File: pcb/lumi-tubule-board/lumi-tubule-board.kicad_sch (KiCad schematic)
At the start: 44 parts, among them SW1 SWITCH_TACT_SMT4.6X2.8, SW2 SWITCH_TACT_SMT4.6X2.8, U1 SHTC3, U2 VREG_SOT23-5, U3 ESP32-S3-MINI-1, U4 LIS2Dx12, U5 TLC59108xPW, U6 TLC59108xPW, X1 USB_C

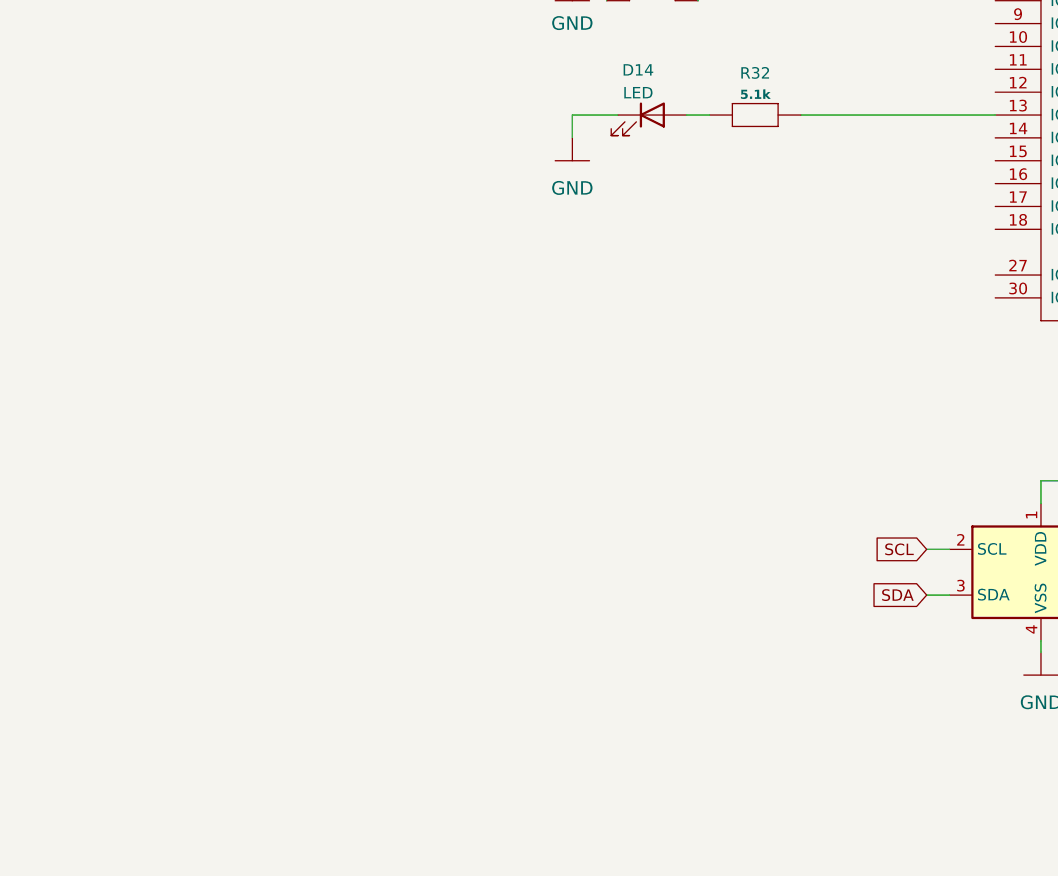
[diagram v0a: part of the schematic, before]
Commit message: Add USB data/power splitter board
Add a small separate (mousebites) USB power/data splitter board. Fits neatly within the central cutout of the main board.
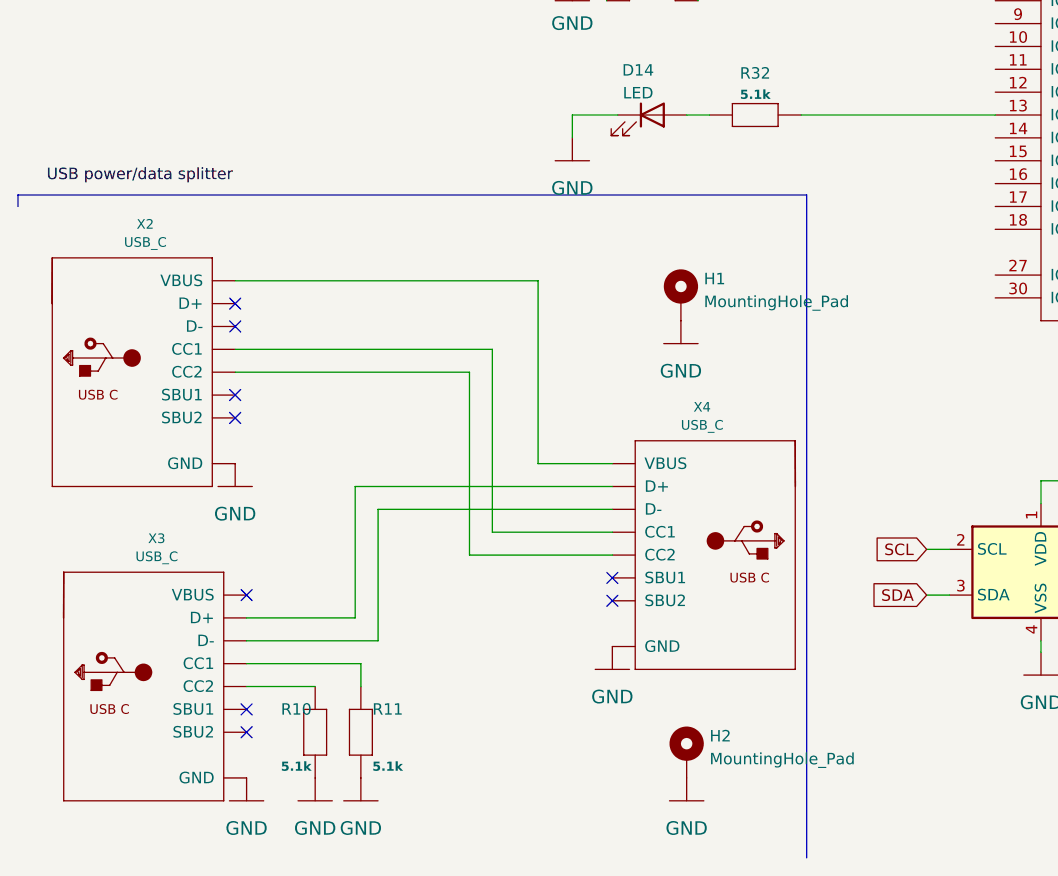
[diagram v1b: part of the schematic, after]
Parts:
- added H1, H2: MountingHole_Pad, symbol Mechanical:MountingHole_Pad
- added R10, R11: 5.1k, Resistor_SMD:R_0603_1608Metric, symbol Adafruit_ESP32-S3_8MB_No_PSRAM-eagle-import:RESISTOR_0603
- added X2, X3, X4: USB_C, Connector_USB:USB_C_Receptacle_HRO_TYPE-C-31-M-12, symbol Adafruit_ESP32-S3_8MB_No_PSRAM-eagle-import:USB_C
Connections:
- net GND: now also H1.1, H2.1, R10.2, R11.2, X2.A1 (GND), X2.A12 (GND), X2.B1 (GND), X2.B12 (GND), X3.A1 (GND), X3.A12 (GND), X3.B1 (GND), X3.B12 (GND), X4.A1 (GND), X4.A12 (GND), X4.B1 (GND), X4.B12 (GND)
- new net: X2.A4 (VBUS), X2.A9 (VBUS), X2.B4 (VBUS), X2.B9 (VBUS), X4.A4 (VBUS), X4.A9 (VBUS), X4.B4 (VBUS), X4.B9 (VBUS)
- new net: X2.A5 (CC1), X4.A5 (CC1)
- new net: X3.A6 (D+), X3.B6 (D+), X4.A6 (D+), X4.B6 (D+)
- new net: X3.A7 (D-), X3.B7 (D-), X4.A7 (D-), X4.B7 (D-)
- new net: X2.B5 (CC2), X4.B5 (CC2)
- new net: X2.A6 (D+), X2.B6 (D+)
- new net: X2.A7 (D-), X2.B7 (D-)
- new net: R10.1, X3.B5 (CC2)
- new net: X3.A4 (VBUS), X3.A9 (VBUS), X3.B4 (VBUS), X3.B9 (VBUS)
- new net: R11.1, X3.A5 (CC1)
- no-connect marks 8 -> 17

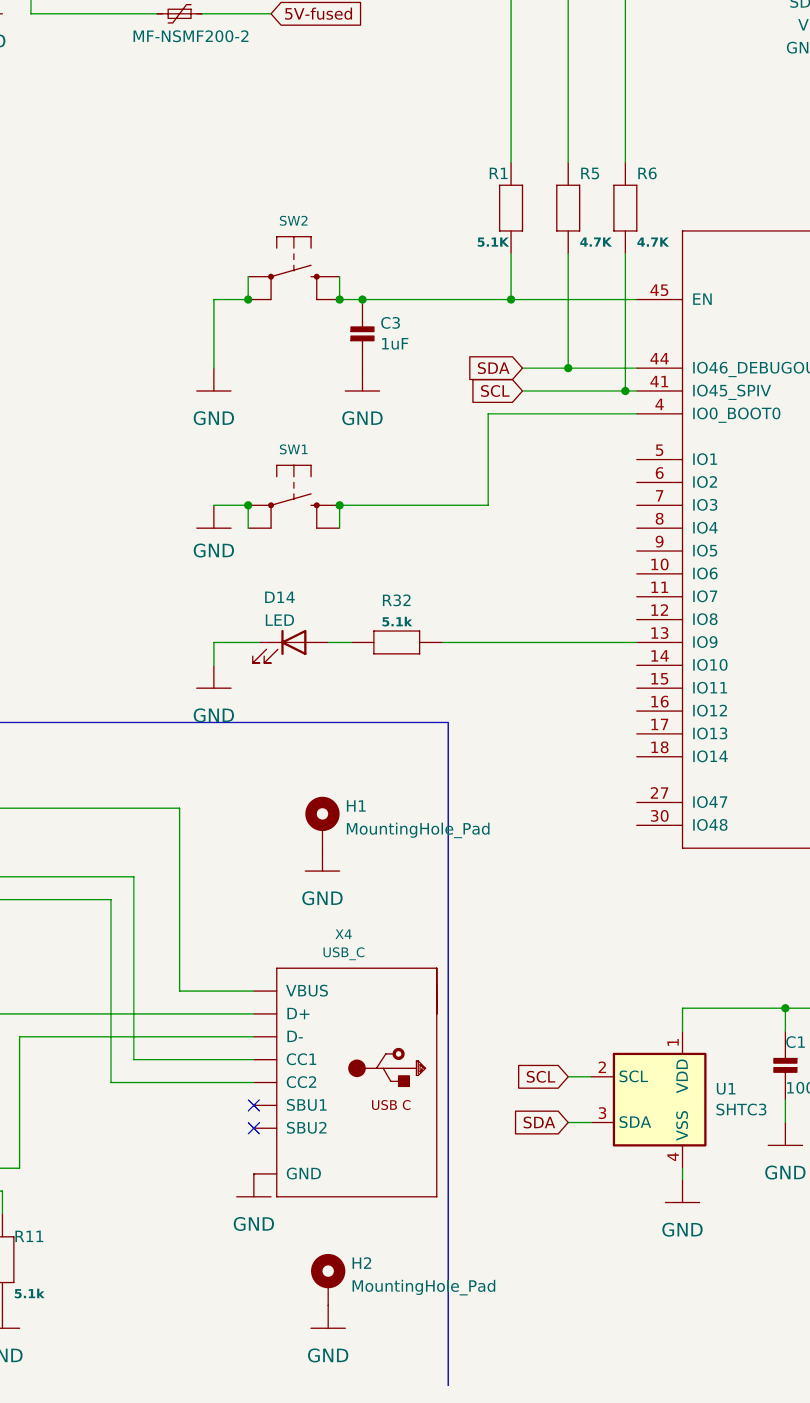
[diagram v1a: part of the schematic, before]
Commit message: Finalise fabrication output
Minor changes, fixes to BOM and schematic footprints.
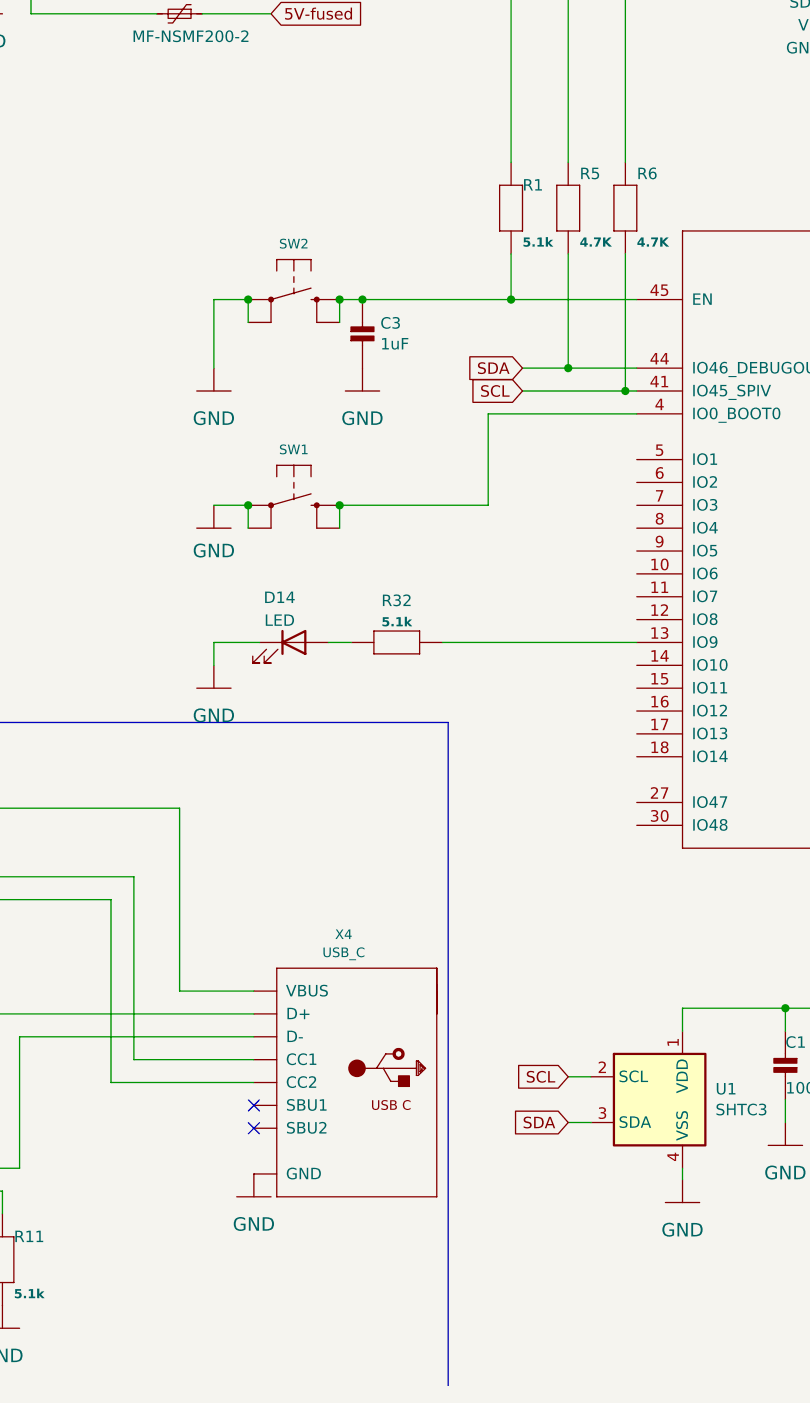
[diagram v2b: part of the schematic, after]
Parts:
- removed H1, H2: MountingHole_Pad, symbol Mechanical:MountingHole_Pad
- removed R1: 5.1K, Resistor_SMD:R_0805_2012Metric, symbol Adafruit_ESP32-S3_8MB_No_PSRAM-eagle-import:RESISTOR_0603_NOOUT
- added R1: 5.1k, Resistor_SMD:R_0603_1608Metric, symbol Adafruit_ESP32-S3_8MB_No_PSRAM-eagle-import:RESISTOR_0603
- 2A-8V1: JLCPCB ref (none) -> C89656
- SW1, SW2: footprint lumi-tubule-board:BTN_KMR2_4.6X2.8 -> lumi-tubule-board:Button_switch_TS342A2P; JLCPCB ref (none) -> C557591
- X1, X2, X3, X4: JCLPCB ref C2760486 -> (none); JLCPCB ref (none) -> C2760486
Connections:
- net 3.3V: now also R1.1
- net at C3.1, SW2.B (S), SW2.B' (S1)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: now also R1.2
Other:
- moved on the sheet: SW2

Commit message: Produced PCB files
PCB version 0.1.1 files. Corrected one error in production regarding voltage regulator.
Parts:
- U2: JLCPCB ref C176944 -> C51118; notes (none) -> 3.3V variant
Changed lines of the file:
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@@
       (effects (font (size 1.27 1.27)) hide)
     )
-    (property "JLCPCB ref" "C176944" (id 4) (at 80.01 26.67 0)
+    (property "JLCPCB ref" "C51118" (id 4) (at 80.01 26.67 0)
       (effects (font (size 1.27 1.27)) hide)
     )
+    (property "notes" "3.3V variant" (id 5) (at 80.01 26.67 0)
+      (effects (font (size 1.27 1.27)) hide)
+    )

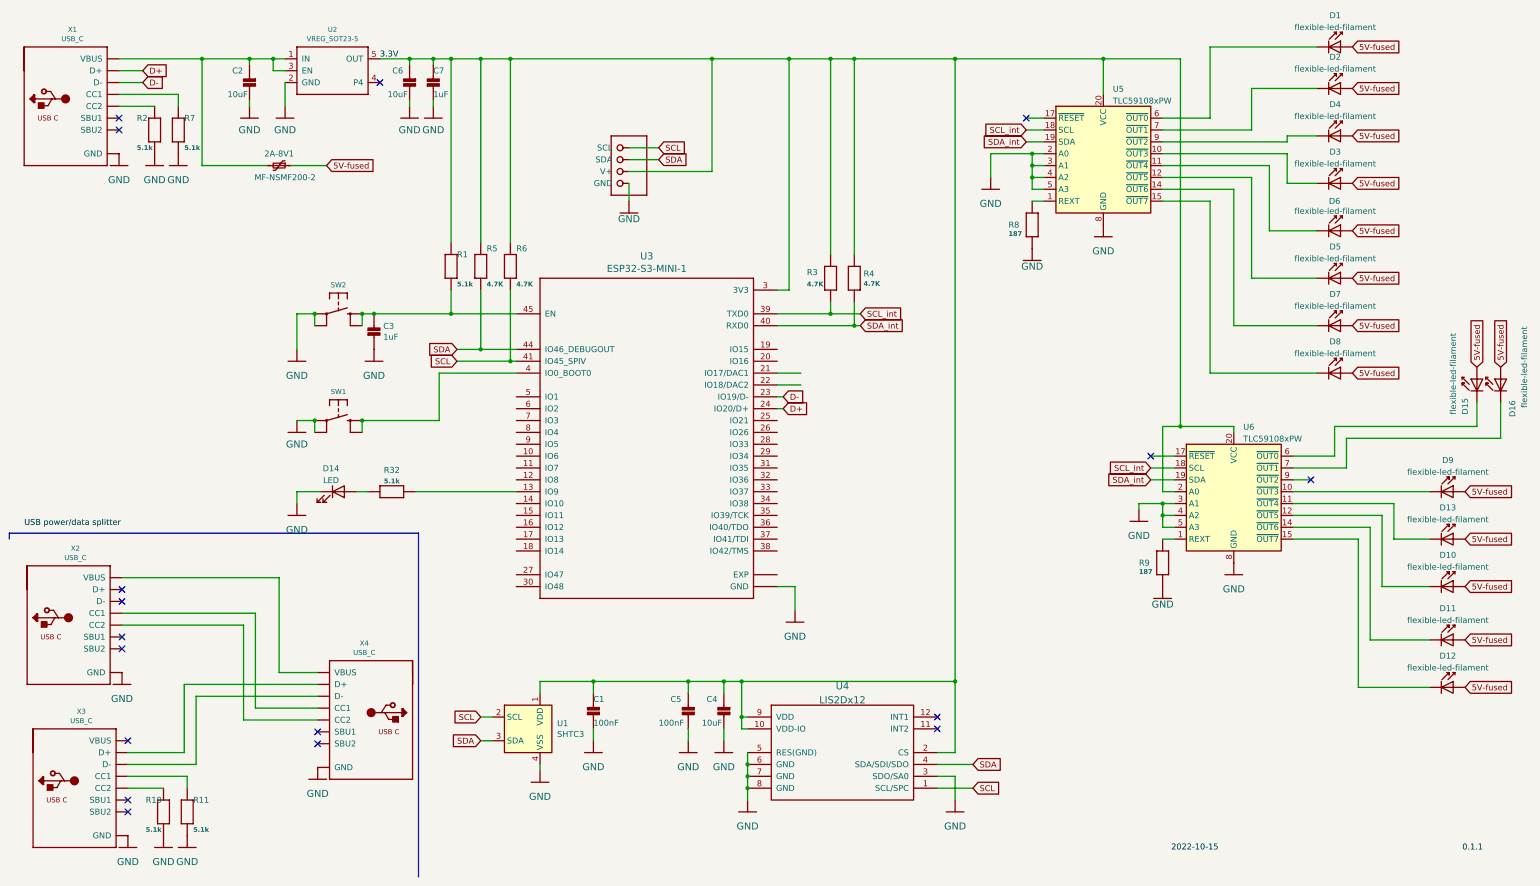
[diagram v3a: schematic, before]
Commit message: PCB V0.1.2
Fixed some big issues with the USB type-C connector traces. Annotated all the nets so PCB is easier to follow. Still strange issue with fills in the buddy USB board.
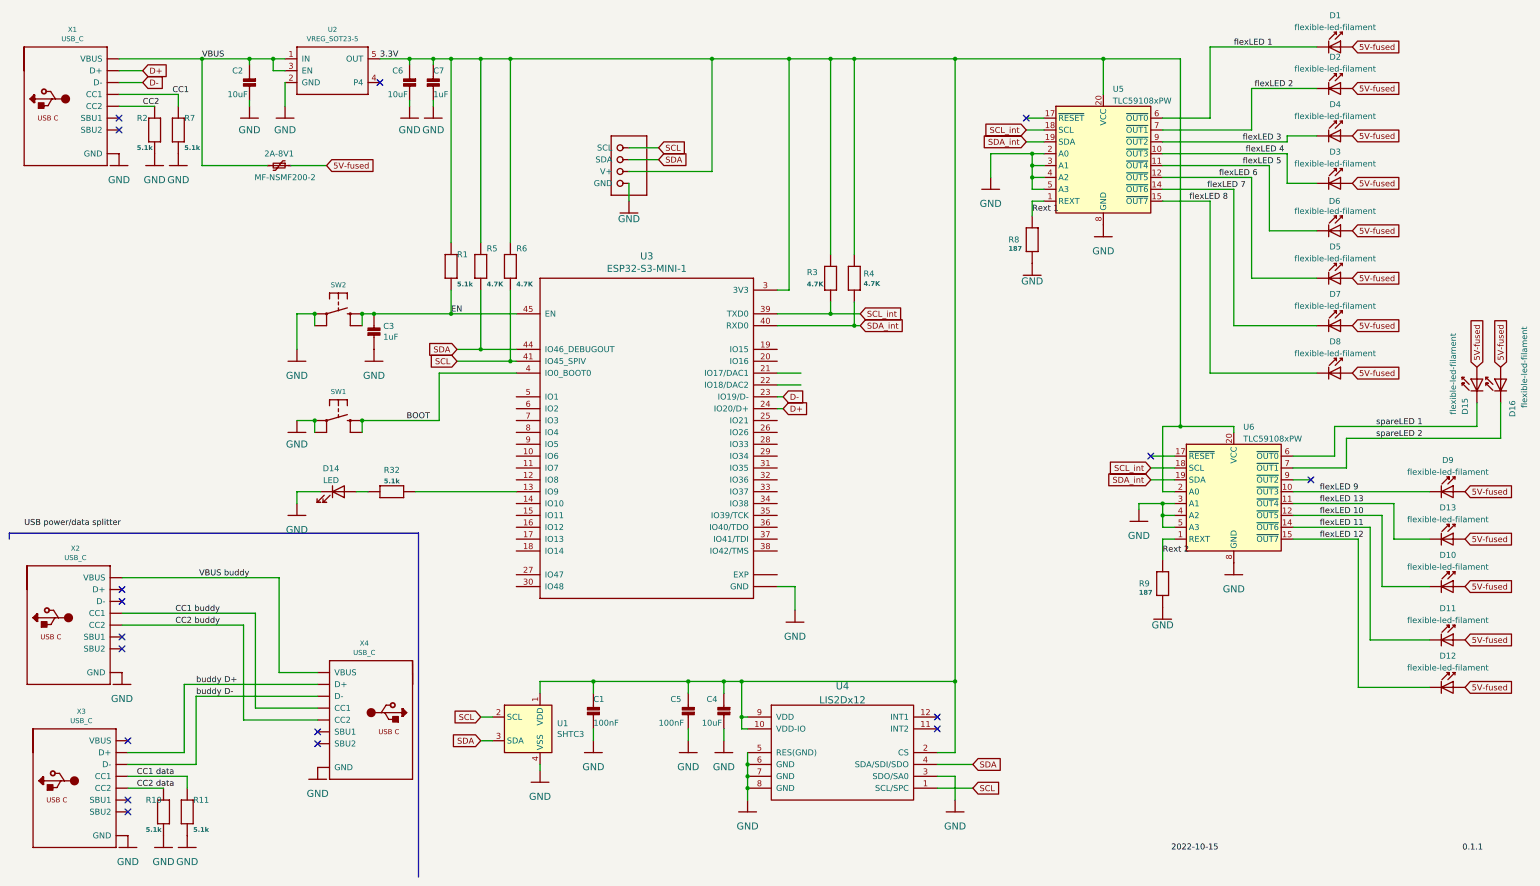
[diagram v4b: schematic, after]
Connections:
- net BOOT: now reaches SW1.B (S), SW1.B' (S1), U3.4 (IO0_BOOT0)
- net EN: now reaches C3.1, R1.2, SW2.B (S), SW2.B' (S1), U3.45 (EN)
- net VBUS: now reaches 2A-8V1.2, C2.2, U2.1 (IN), U2.3 (EN), X1.A4 (VBUS), X1.A9 (VBUS), X1.B4 (VBUS), X1.B9 (VBUS)
- net CC1: now reaches R7.1, X1.A5 (CC1)
- net CC2: now reaches R2.1, X1.B5 (CC2)
- net flexLED 13: now reaches D13.1 (K), U6.11 (~{OUT4})
- net flexLED 1: now reaches D1.1 (K), U5.6 (~{OUT0})
- net spareLED 2: now reaches D16.1 (K), U6.7 (~{OUT1})
- net Rext 1: now reaches R8.1, U5.1 (REXT)
- net Rext 2: now reaches R9.1, U6.1 (REXT)
- net VBUS buddy: now reaches X2.A4 (VBUS), X2.A9 (VBUS), X2.B4 (VBUS), X2.B9 (VBUS), X4.A4 (VBUS), X4.A9 (VBUS), X4.B4 (VBUS), X4.B9 (VBUS)
- net CC1 buddy: now reaches X2.A5 (CC1), X4.A5 (CC1)
- net buddy D+: now reaches X3.A6 (D+), X3.B6 (D+), X4.A6 (D+), X4.B6 (D+)
- net buddy D-: now reaches X3.A7 (D-), X3.B7 (D-), X4.A7 (D-), X4.B7 (D-)
- net CC2 buddy: now reaches X2.B5 (CC2), X4.B5 (CC2)
- net flexLED 2: now reaches D2.1 (K), U5.7 (~{OUT1})
- net flexLED 4: now reaches D3.1 (K), U5.10 (~{OUT3})
- net flexLED 5: now reaches D6.1 (K), U5.11 (~{OUT4})
- net flexLED 6: now reaches D5.1 (K), U5.12 (~{OUT5})
- net flexLED 7: now reaches D7.1 (K), U5.14 (~{OUT6})
- net flexLED 8: now reaches D8.1 (K), U5.15 (~{OUT7})
- net flexLED 3: now reaches D4.1 (K), U5.9 (~{OUT2})
- net flexLED 11: now reaches D11.1 (K), U6.14 (~{OUT6})
- net flexLED 9: now reaches D9.1 (K), U6.10 (~{OUT3})
- net flexLED 10: now reaches D10.1 (K), U6.12 (~{OUT5})
- net flexLED 12: now reaches D12.1 (K), U6.15 (~{OUT7})
- net spareLED 1: now reaches D15.1 (K), U6.6 (~{OUT0})
- net CC2 data: now reaches R10.1, X3.B5 (CC2)
- net CC1 data: now reaches R11.1, X3.A5 (CC1)
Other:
- moved on the sheet: R8, R9
